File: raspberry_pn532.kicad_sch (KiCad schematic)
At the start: 2 parts, among them J1 Raspberry_Pi_zero_2w

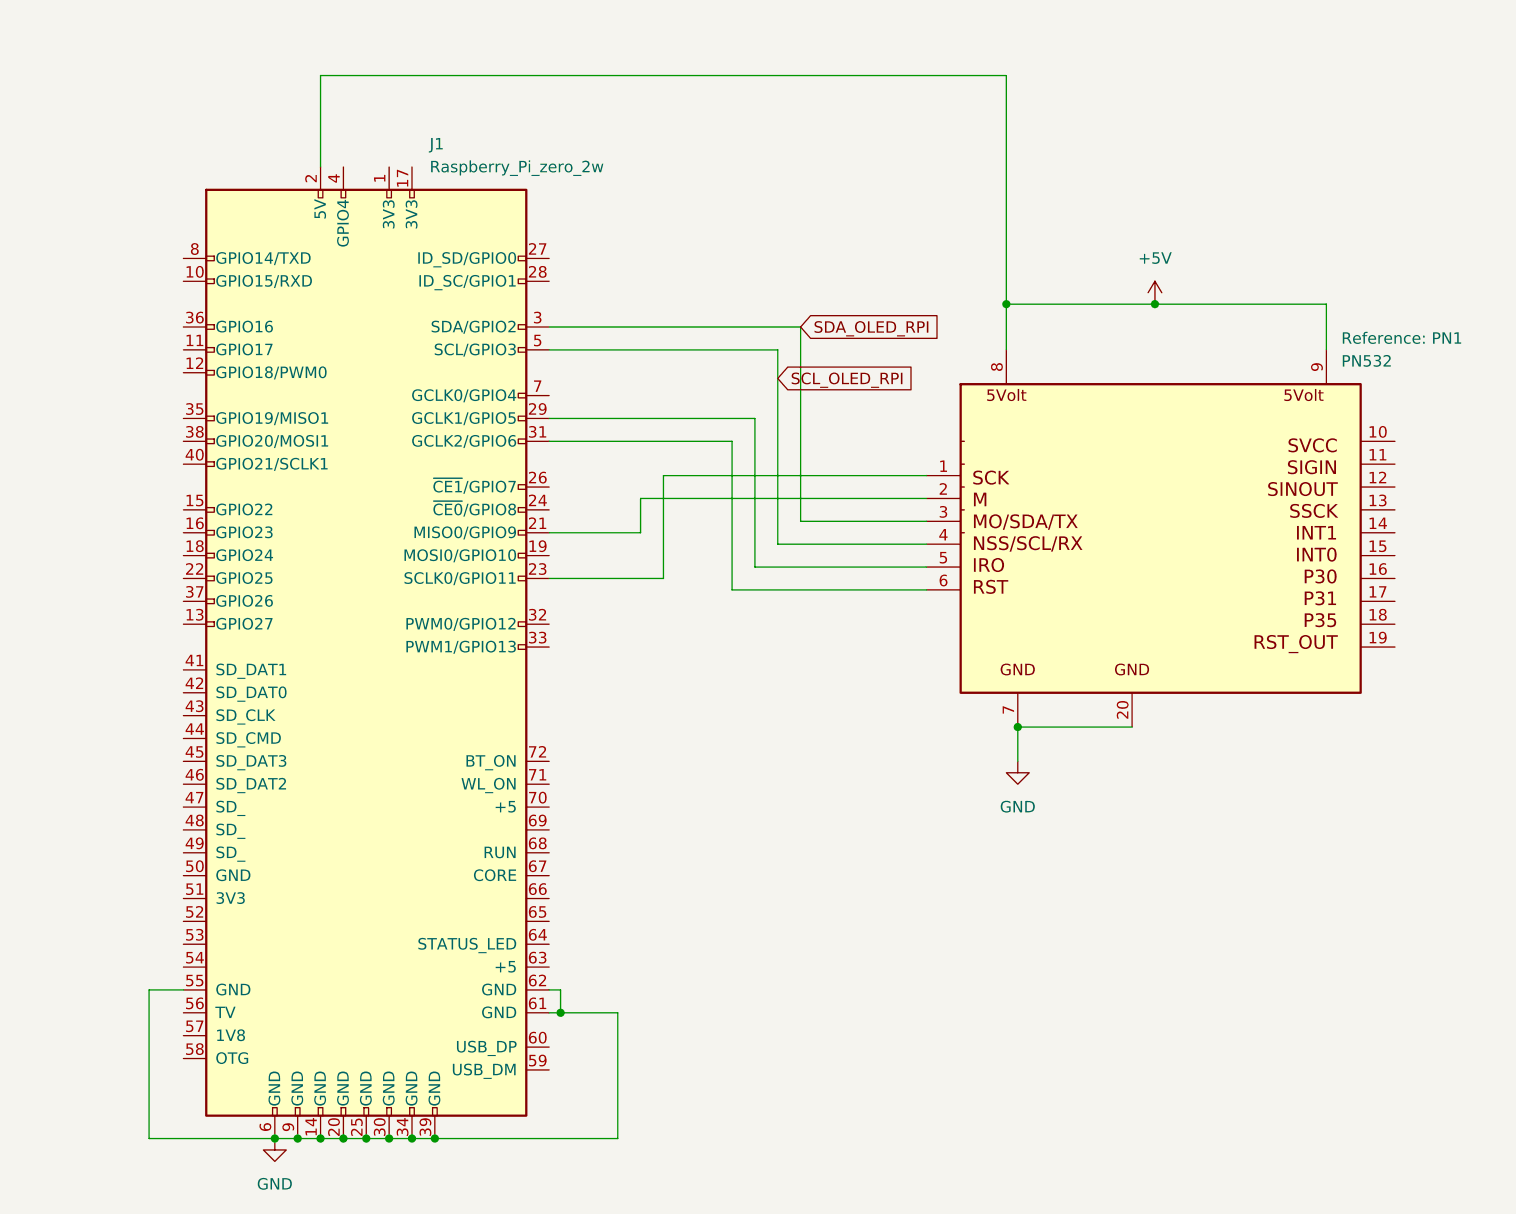
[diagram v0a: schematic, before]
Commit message: Add hierarchical labels for ALL PN532 pins (22 pins, _PN532 suffix)
Each pin of PN2 now has a hierarchical label with name matching the pin
plus _PN532 suffix (e.g. SCK_PN532, INT_PN532, GND_PN532)
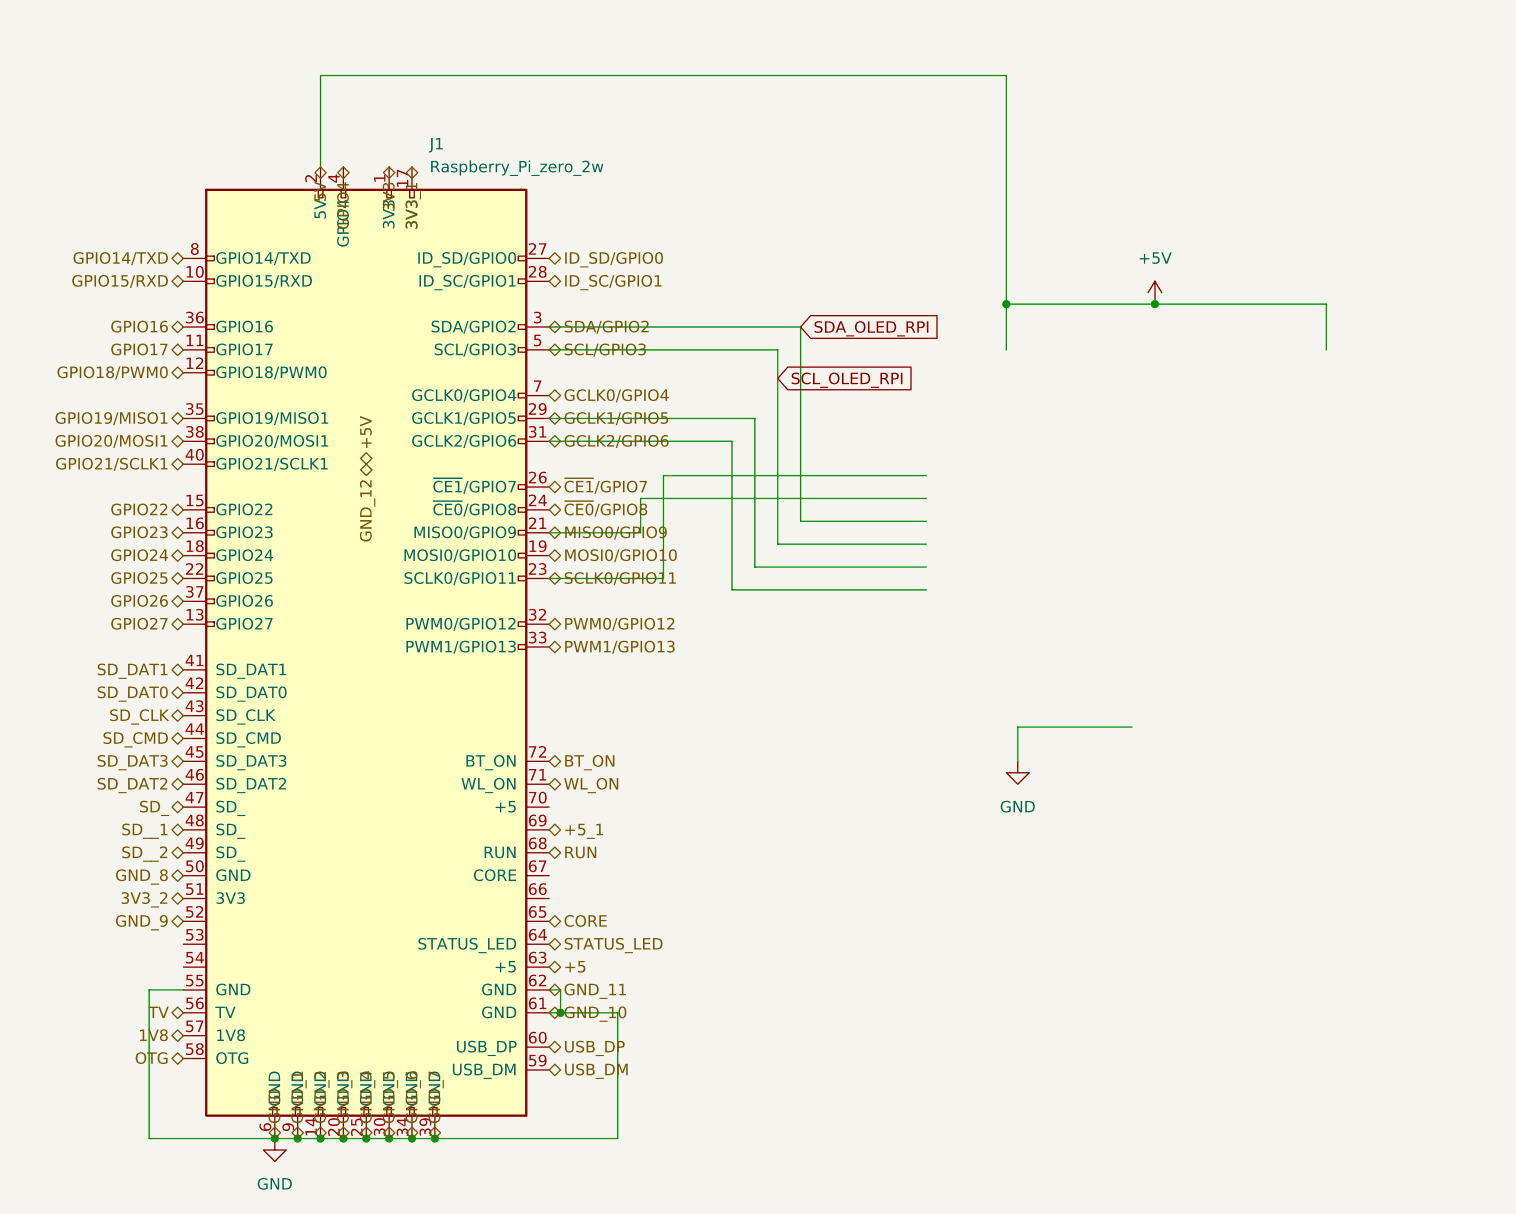
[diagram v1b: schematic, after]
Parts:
- removed PN1: PN532, Connector_PinSocket_2.54mm:PinSocket_1x08_P2.54mm_Vertical, symbol Device:PN532
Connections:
- net SCLK0/GPIO11: now reaches J1.23 (SCLK0/GPIO11)
- net MISO0/GPIO9: now reaches J1.21 (MISO0/GPIO9)
- net GCLK1/GPIO5: now reaches J1.29 (GCLK1/GPIO5)
- net GCLK2/GPIO6: now reaches J1.31 (GCLK2/GPIO6)
- net 3V3: now reaches J1.1 (3V3)
- net GPIO15/RXD: now reaches J1.10 (GPIO15/RXD)
- net GPIO17: now reaches J1.11 (GPIO17)
- net GPIO18/PWM0: now reaches J1.12 (GPIO18/PWM0)
- net GPIO27: now reaches J1.13 (GPIO27)
- net GPIO22: now reaches J1.15 (GPIO22)
- net GPIO23: now reaches J1.16 (GPIO23)
- net 3V3_1: now reaches J1.17 (3V3)
- net GPIO24: now reaches J1.18 (GPIO24)
- net MOSI0/GPIO10: now reaches J1.19 (MOSI0/GPIO10)
- net GPIO25: now reaches J1.22 (GPIO25)
- net ~{CE0}/GPIO8: now reaches J1.24 (~{CE0}/GPIO8)
- net ~{CE1}/GPIO7: now reaches J1.26 (~{CE1}/GPIO7)
- net ID_SD/GPIO0: now reaches J1.27 (ID_SD/GPIO0)
- net ID_SC/GPIO1: now reaches J1.28 (ID_SC/GPIO1)
- net PWM0/GPIO12: now reaches J1.32 (PWM0/GPIO12)
- net PWM1/GPIO13: now reaches J1.33 (PWM1/GPIO13)
- net GPIO19/MISO1: now reaches J1.35 (GPIO19/MISO1)
- net GPIO16: now reaches J1.36 (GPIO16)
- net GPIO26: now reaches J1.37 (GPIO26)
- net GPIO20/MOSI1: now reaches J1.38 (GPIO20/MOSI1)
- net GPIO4: now reaches J1.4 (GPIO4)
- net GPIO21/SCLK1: now reaches J1.40 (GPIO21/SCLK1)
- net SD_DAT1: now reaches J1.41 (SD_DAT1)
- net SD_DAT0: now reaches J1.42 (SD_DAT0)
- net SD_CLK: now reaches J1.43 (SD_CLK)
- net SD_CMD: now reaches J1.44 (SD_CMD)
- net SD_DAT3: now reaches J1.45 (SD_DAT3)
- net SD_DAT2: now reaches J1.46 (SD_DAT2)
- net SD_: now reaches J1.47 (SD_)
- net SD__1: now reaches J1.48 (SD_)
- net SD__2: now reaches J1.49 (SD_)
- net GND_8: now reaches J1.50 (GND)
- net 3V3_2: now reaches J1.51 (3V3)
- net GND_9: now reaches J1.52
- net TV: now reaches J1.56 (TV)
- net 1V8: now reaches J1.57 (1V8)
- net OTG: now reaches J1.58 (OTG)
- net USB_DM: now reaches J1.59 (USB_DM)
- net USB_DP: now reaches J1.60 (USB_DP)
- net +5: now reaches J1.63 (+5)
- net STATUS_LED: now reaches J1.64 (STATUS_LED)
- net CORE: now reaches J1.65
- net RUN: now reaches J1.68 (RUN)
- net +5_1: now reaches J1.69
- net GCLK0/GPIO4: now reaches J1.7 (GCLK0/GPIO4)
- net WL_ON: now reaches J1.71 (WL_ON)
- net BT_ON: now reaches J1.72 (BT_ON)
- net GPIO14/TXD: now reaches J1.8 (GPIO14/TXD)

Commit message: Remove all GND hierarchical pins and labels from all sheets
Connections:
- net GND_8: no longer names the net of J1.50 (GND)
- net GND_9: no longer names the net of J1.52
- net SCL_OLED_RPI renamed SCL/GPIO3
- net SDA_OLED_RPI renamed SDA/GPIO2
